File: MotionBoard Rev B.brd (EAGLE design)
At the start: 99 x 53.3 mm, 89 parts, among them IC1 LPC1769, IC2 LD1117, Q1 BSL207SP, Q2 12MHz, Q3 25MHz, U1 ARDUINO-FIREPICK+RAMPS, X1 ST9S008V4AR1500

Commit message: Update board files
Signed-off-by: Paul Jones <paul@pauljones.id.au>
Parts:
- removed C45, C50, C64: 10uF, SparkFun:EIA3216
- removed C48: 1uF, SparkFun:EIA3216
- removed JP4: MICRO-USB-FCI-10103592, micro-usb-fci-10103592:MICRO-USB-FCI-10103592
- removed S1, S2, S3, S4: (no value), SparkFun:TACTILE_SWITCH_SMD
- added C10, C17, C18: 1u, iwt:0603
- added C16: 100n, iwt:0603
- added C19, C20, C6, C7: 10u, iwt:0603
- added DFU: SW3, iwt:TOGGLE-SW-SMD
- added ISP: SW2, iwt:TOGGLE-SW-SMD
- added RST: SW1, iwt:TOGGLE-SW-SMD
- added X2: USB-MICRO-B, iwt:FCI-10118194-0001LF
- C1, C15, C44, C46, C51, C52, C53: value .1uF -> 100n; device resistor:C0603 -> iwt:0603
- C11: value .1uF -> 100n
- C12, C13, C14, C8: value .1uF -> 100n; device rcl:C0603 -> iwt:0603
- C2, C3, C4, C5: value 18pF -> 18p; device rcl:C0603 -> iwt:0603
- C49: value 470pF -> 470p; device resistor:C0603K -> iwt:0603
- C54, C55, C56, C57, C58, C59: value 18pF -> 18p; device resistor:C0603 -> iwt:0603
- C9: value 10uF -> 100n; device SparkFun:EIA3216 -> iwt:0603
- D1: value DIODE-SMB -> MBR0530; device iwt:SMB -> SparkFun-DiscreteSemi:SOD-123
- IC1: value LPC1769 -> LPC1769FBD100 or LPC4078FBD100E; device microbuilder:LQFP100 -> iwt:LQFP100
- moved LED1 69.2 mm to (70.7, 10.6)
- moved LED2 63.3 mm to (67.5, 10.6)
- moved LED3 57.4 mm to (64.2, 10.6)
- moved LED4 51.6 mm to (61.0, 10.6)
- moved R11 49.3 mm to (67.1, 18.9), turned to 90 degrees
- moved R12 48.4 mm to (65.6, 18.9), turned to 90 degrees
- moved R13 47.6 mm to (64.2, 18.9), turned to 90 degrees
- moved R10 45.4 mm to (68.5, 18.9)
- moved R14 33.3 mm to (57.8, 10.8)
- moved LED5 32.9 mm to (55.7, 10.6)
- moved C8 15.9 mm to (7.92, 6.30), turned to 180 degrees
- moved R50 13.5 mm to (10.8, 43.9), turned to 0 degrees
- moved LOGO6 10.2 mm to (88.8, 31.8)
- moved LOGO4 9.86 mm to (88.8, 13.2)
- moved LOGO10 9.77 mm to (88.2, 28.4)
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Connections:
- removed net N$61: JP4.3, R8.1
- removed net N$62: JP4.2, R9.1
- new net D_N: R9.1, X2.2
- new net D_P: R8.1, X2.3
- net !RST: now also RST.3, RST.4; no longer S1.1, S1.2, S3.1, S3.2
- net 3.3V: now also C19.1, C20.1, C7.1, C9.1, IC1.13; no longer C50.A, C9.A
- net 5V: now also C16.1, C17.1, C18.1; no longer C64.A
- net GND: now also C10.2, C16.2, C17.2, C18.2, C19.2, C20.2, C6.2, C7.2, C9.2, DFU.1, DFU.2, DFU.GND, ISP.1, ISP.2, ISP.GND, RST.1, RST.2, RST.GND, X2.5, X2.S1, X2.S10, X2.S11, X2.S12, X2.S2, X2.S3, X2.S4, X2.S5, X2.S6, X2.S7, X2.S8, X2.S9; no longer C45.C, C48.C, C50.C, C64.C, C9.C, JP4.5, S1.3, S1.4, S2.3, S2.4, S3.3, S3.4, S4.3, S4.4
- net N$12: now also C10.1; no longer C48.A
- net N$9: now also X2.1; no longer JP4.1
- net P2[10]: now also ISP.3, ISP.4; no longer S2.1, S2.2, S4.1, S4.2
- net P2[12]: now also DFU.3, DFU.4
- net VDD: now also C6.1; no longer C45.A
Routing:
- net P2[12]: track 52.2 -> 132.3 mm, vias 0 -> 6
- net P2[10]: track 69.2 -> 142.0 mm, vias 2 -> 8
- net P1[21]: track 66.6 -> 21.7 mm
- net P1[20]: track 64.0 -> 21.4 mm
- net P1[19]: track 60.0 -> 21.3 mm
- net P1[18]: track 52.3 -> 19.0 mm
- net !RST: track 110.3 -> 134.0 mm, vias 3 -> 4
- net N$87: track 26.1 -> 6.61 mm, vias 0 -> 2
- net N$61: track 18.3 -> 0.00 mm
- net N$62: track 17.4 -> 0.00 mm
- net VDD: track 17.1 -> 28.8 mm, vias 3 -> 5
- net N$68: track 2.37 -> 12.7 mm
- net GND: track 80.8 -> 70.5 mm, vias 60 -> 81
- net 5V: track 189.8 -> 179.8 mm
- net N$86: track 15.7 -> 5.85 mm, vias 0 -> 2
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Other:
- board text added: "1 2 3 4"
- board text added: "DFU"
- board text added: "Designed in Australia by Paul Jones"
- board text added: "FTDI"
- board text added: "MotionBoard"
- board text added: "Power"
- board text added: "Smoothie and Ramps 1.4 Compatible - Rev B"
- board text removed: "(Smoothie Compatible)"
- board text removed: "4 3 2 1"
- board text removed: "FireSmoo CPU Module"
- board text removed: "Rev B"

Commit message: Cosmetic changes
Add new name to schematic and rearrange page 1 so it all fits on the
page
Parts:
- removed LOGO4: LOGO-FIREPICKMEDIUM, FirePick:LOGO-FIREPICK-MEDIUM
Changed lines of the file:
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@@
 </element>
 <element name="LOGO10" library="FirePick" package="LOGO-OSHW-SMALL" value="LOGO-OSHWSMALL" x="88.1888" y="28.3972" smashed="yes" rot="R90"/>
-<element name="LOGO4" library="FirePick" package="LOGO-FIREPICK-MEDIUM" value="LOGO-FIREPICKMEDIUM" x="88.7984" y="13.208" smashed="yes" rot="R90"/>
 <element name="LOGO6" library="FirePick" package="LOGO-CC-BY-SA-MEDIUM" value="LOGO-CC-BY-SAMEDIUM" x="88.7984" y="31.75" smashed="yes" rot="R90"/>
 <element name="Q1" library="transistor-fet" package="SC74_INFINEON" value="BSL207SP" x="33.3248" y="42.2656" smashed="yes" rot="R90">

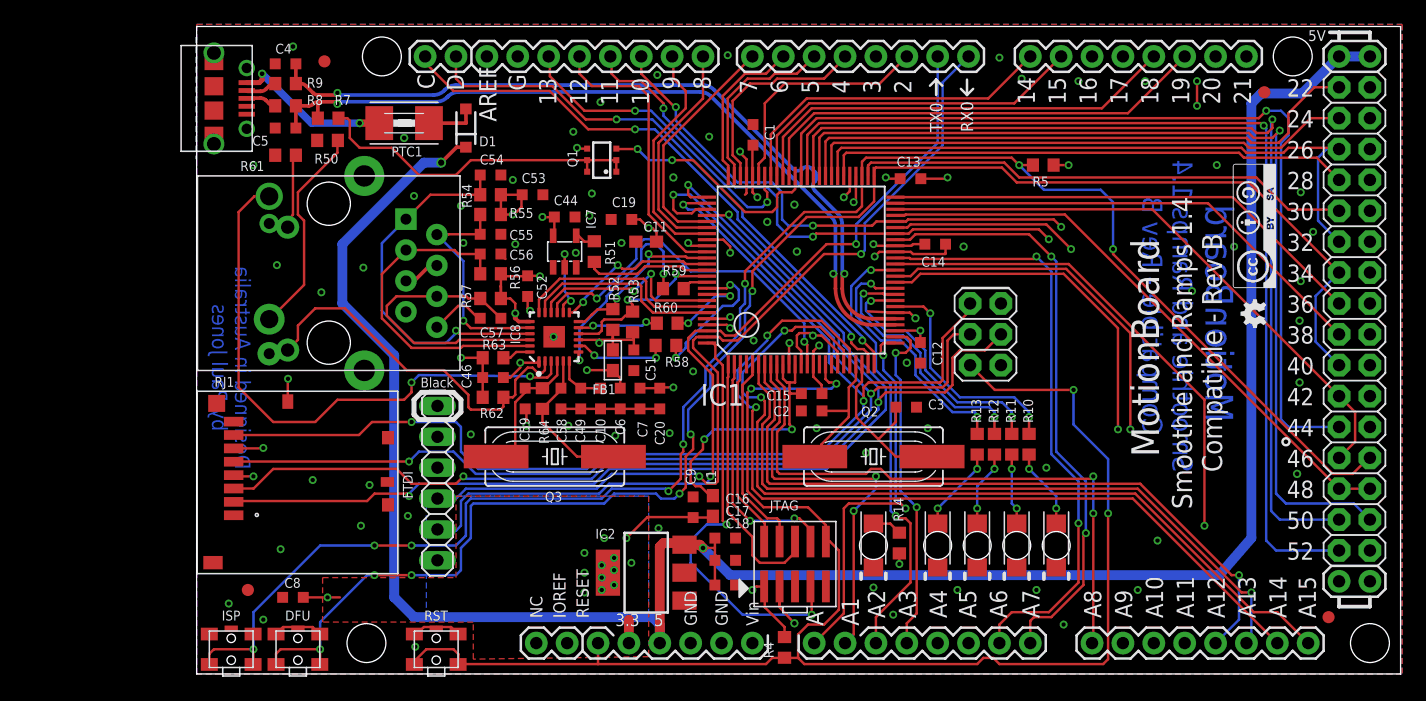
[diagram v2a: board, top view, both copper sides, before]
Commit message: Update with production files
Also note a "whoopsie" where wire jumpers are required...
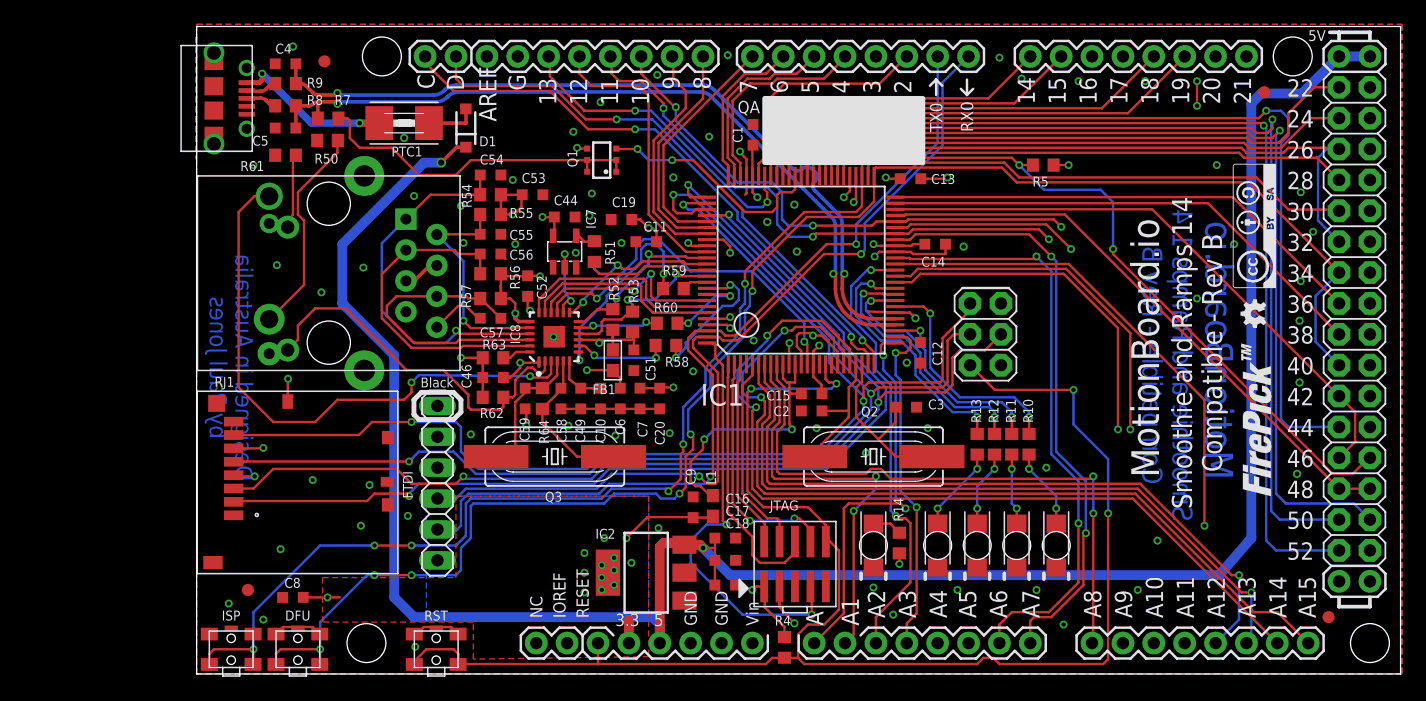
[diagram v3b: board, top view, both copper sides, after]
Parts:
- added LOGO4: LOGO-FIREPICKMEDIUM, FirePick:LOGO-FIREPICK-MEDIUM
- C11: device rcl:C0603 -> iwt:0603
- L1: value (none) -> 10uH
- Q1: value BSL207SP -> NTGS3441T1G
- R51, R58, R59, R60: value 22R -> 33R
- R52: value 1.5K -> 1.5k
- R53, R62: value 10K -> 10k
- R63: value 12.1K -> 12.1k
- R7: value 1K -> 1.5k
- U1: device EARM01:ARDUINO_MEGA_NEW -> iwt:ARDUINO_MEGA_NEW
- moved LOGO2 4.89 mm to (74.0, 25.1)
- moved LOGO3 3.87 mm to (73.4, 29.3)
- moved LOGO1 2.87 mm to (74.0, 11.4)
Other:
- board text added: "MotionBoard.io"
- board text added: "QA"
- board text removed: "MotionBoard"

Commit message: Update component values
Signed-off-by: Paul Jones <paul@pauljones.id.au>
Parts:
- L1: value 10uH -> (none)
- Q1: value NTGS3441T1G -> BSL207SP
- R51, R58, R59, R60: value 33R -> 22R
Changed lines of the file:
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@@
 <attribute name="VALUE" x="45.9312" y="4.7959" size="0.4064" layer="27"/>
 </element>
-<element name="L1" library="SparkFun" package="0603" value="10uH" x="42.4688" y="13.8176" smashed="yes" rot="R270">
+<element name="L1" library="SparkFun" package="0603" value="" x="42.4688" y="13.8176" smashed="yes" rot="R270">
 <attribute name="NAME" x="42.7228" y="15.5702" size="0.8128" layer="25" font="vector" rot="R90"/>
 <attribute name="VALUE" x="41.3258" y="14.8336" size="0.4064" layer="27" font="vector" rot="R270"/>
@@
 <element name="LOGO10" library="FirePick" package="LOGO-OSHW-SMALL" value="LOGO-OSHWSMALL" x="88.1888" y="28.3972" smashed="yes" rot="R90"/>
 <element name="LOGO6" library="FirePick" package="LOGO-CC-BY-SA-MEDIUM" value="LOGO-CC-BY-SAMEDIUM" x="88.7984" y="31.75" smashed="yes" rot="R90"/>
-<element name="Q1" library="transistor-fet" package="SC74_INFINEON" value="NTGS3441T1G" x="33.3248" y="42.2656" smashed="yes" rot="R90">
+<element name="Q1" library="transistor-fet" package="SC74_INFINEON" value="BSL207SP" x="33.3248" y="42.2656" smashed="yes" rot="R90">
 <attribute name="NAME" x="31.3184" y="41.6752" size="0.8128" layer="25" rot="R90"/>
 <attribute name="VALUE" x="36.2248" y="41.0656" size="1.27" layer="27" rot="R90"/>
@@
 <attribute name="VALUE" x="9.8806" y="41.8592" size="1.27" layer="27"/>
 </element>
-<element name="R51" library="resistor" package="R0603" value="33R" x="32.7152" y="34.7472" smashed="yes" rot="R270">
+<element name="R51" library="resistor" package="R0603" value="22R" x="32.7152" y="34.7472" smashed="yes" rot="R270">
 <attribute name="NAME" x="33.6042" y="35.6362" size="0.8128" layer="25" rot="R270"/>
 <attribute name="VALUE" x="30.6832" y="35.6362" size="1.27" layer="27" rot="R270"/>
@@
 <attribute name="VALUE" x="25.0698" y="32.9184" size="1.27" layer="27" rot="R180"/>
 </element>
-<element name="R58" library="resistor" package="R0603" value="33R" x="38.608" y="27.0256" smashed="yes">
+<element name="R58" library="resistor" package="R0603" value="22R" x="38.608" y="27.0256" smashed="yes">
 <attribute name="NAME" x="38.5318" y="25.273" size="0.8128" layer="25"/>
 <attribute name="VALUE" x="37.719" y="24.9936" size="1.27" layer="27"/>
 </element>
-<element name="R59" library="resistor" package="R0603" value="33R" x="39.2176" y="31.6992" smashed="yes">
+<element name="R59" library="resistor" package="R0603" value="22R" x="39.2176" y="31.6992" smashed="yes">
 <attribute name="NAME" x="38.3286" y="32.7914" size="0.8128" layer="25"/>
 <attribute name="VALUE" x="38.3286" y="29.6672" size="1.27" layer="27"/>
 </element>
-<element name="R60" library="resistor" package="R0603" value="33R" x="38.7096" y="28.8544" smashed="yes">
+<element name="R60" library="resistor" package="R0603" value="22R" x="38.7096" y="28.8544" smashed="yes">
 <attribute name="NAME" x="37.6174" y="29.7434" size="0.8128" layer="25"/>
 <attribute name="VALUE" x="37.8206" y="26.8224" size="1.27" layer="27"/>
